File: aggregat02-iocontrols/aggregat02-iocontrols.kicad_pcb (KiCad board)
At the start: 2 copper layers, 45.7 x 101.9 mm, 75 parts, among them Q2 Q_NPN_BEC

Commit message: v1.0"
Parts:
- removed D2: LED, LED_THT:LED_D3.0mm
- added J1: Conn_01x04, Connector_PinHeader_2.54mm:PinHeader_1x04_P2.54mm_Vertical, B.Cu at (78.7, 69.3)
- added J10: Conn_01x01, Connector_PinHeader_2.54mm:PinHeader_1x01_P2.54mm_Vertical, B.Cu at (81.5, 117.3)
- added J11: Conn_01x01, Connector_PinHeader_2.54mm:PinHeader_1x01_P2.54mm_Vertical, B.Cu at (71.9, 127.0)
- added J12: Conn_01x01, Connector_PinHeader_2.54mm:PinHeader_1x01_P2.54mm_Vertical, B.Cu at (81.8, 127.0)
- added J13: Conn_01x01, Connector_PinHeader_2.54mm:PinHeader_1x01_P2.54mm_Vertical, B.Cu at (71.9, 137.2)
- added J14: Conn_01x01, Connector_PinHeader_2.54mm:PinHeader_1x01_P2.54mm_Vertical, B.Cu at (81.8, 137.2)
- added J15: Conn_01x15, Connector_Molex:Molex_PicoBlade_53047-1510_1x15_P1.25mm_Vertical, B.Cu at (89.2, 57.7)
- added J16: Conn_01x15, Connector_Molex:Molex_PicoBlade_53047-1510_1x15_P1.25mm_Vertical, B.Cu at (88.9, 87.1)
- added J17: Conn_01x03, Connector_PinHeader_2.54mm:PinHeader_1x02_P2.54mm_Vertical, B.Cu at (54.1, 96.8)
- added J18: Conn_01x03, Connector_Molex:Molex_PicoBlade_53047-0310_1x03_P1.25mm_Vertical, B.Cu at (52.8, 55.6)
- added J19: Conn_01x01, Connector_PinHeader_2.54mm:PinHeader_1x01_P2.54mm_Vertical, B.Cu at (56.1, 49.0)
- added J2: Conn_01x04, Connector_PinHeader_2.54mm:PinHeader_1x04_P2.54mm_Vertical, B.Cu at (79.0, 54.6)
- added J3: Conn_01x08, Connector_PinHeader_2.54mm:PinHeader_1x08_P2.54mm_Vertical, B.Cu at (78.7, 86.6)
- added J4: Conn_01x01, Connector_PinHeader_2.54mm:PinHeader_1x01_P2.54mm_Vertical, B.Cu at (51.3, 115.6)
- added J5: Conn_01x01, Connector_PinHeader_2.54mm:PinHeader_1x01_P2.54mm_Vertical, B.Cu at (51.3, 125.5)
- added J6: Conn_01x01, Connector_PinHeader_2.54mm:PinHeader_1x01_P2.54mm_Vertical, B.Cu at (51.3, 135.4)
- added J7: Conn_01x01, Connector_PinHeader_2.54mm:PinHeader_1x01_P2.54mm_Vertical, B.Cu at (79.0, 50.5)
- added J8: Conn_01x01, Connector_PinHeader_2.54mm:PinHeader_1x01_P2.54mm_Vertical, B.Cu at (88.4, 50.8)
- added J9: Conn_01x01, Connector_PinHeader_2.54mm:PinHeader_1x01_P2.54mm_Vertical, B.Cu at (71.9, 117.1)
- added LD11: LED, LED_THT:LED_D3.0mm, F.Cu at (70.9, 112.8)
- added LD12: LED, LED_THT:LED_D3.0mm, F.Cu at (80.8, 112.8)
- added LD21: LED, LED_THT:LED_D3.0mm, F.Cu at (70.9, 122.7)
- added LD22: LED, LED_THT:LED_D3.0mm, F.Cu at (80.8, 122.7)
- added LD31: LED, LED_THT:LED_D3.0mm, F.Cu at (70.9, 132.6)
- added LD32: LED, LED_THT:LED_D3.0mm, F.Cu at (80.8, 132.6)
- added LD_MTR1: LED, LED_THT:LED_D3.0mm, F.Cu at (79.5, 43.7)
- added Q1: Q_NPN_BEC, Package_TO_SOT_SMD:SOT-23, B.Cu at (84.1, 44.7)
- added Q3: Q_NPN_BEC, Package_TO_SOT_SMD:SOT-23, B.Cu at (74.2, 111.3)
- added Q4: Q_NPN_BEC, Package_TO_SOT_SMD:SOT-23, B.Cu at (84.1, 111.5)
- added Q5: Q_NPN_BEC, Package_TO_SOT_SMD:SOT-23, B.Cu at (74.2, 121.2)
- added Q6: Q_NPN_BEC, Package_TO_SOT_SMD:SOT-23, B.Cu at (84.1, 121.2)
- added Q7: Q_NPN_BEC, Package_TO_SOT_SMD:SOT-23, B.Cu at (74.2, 131.3)
- added Q8: Q_NPN_BEC, Package_TO_SOT_SMD:SOT-23, B.Cu at (84.1, 131.3)
- added R42: R 47k 1% 1/8, Resistor_SMD:R_0805_2012Metric_Pad1.15x1.40mm_HandSolder, B.Cu at (85.1, 50.6)
- added R43: R 100k 1% 1/8, Resistor_SMD:R_0805_2012Metric_Pad1.15x1.40mm_HandSolder, B.Cu at (84.1, 47.5)
- added R44: R 270 1% 1/8, Resistor_SMD:R_0805_2012Metric_Pad1.15x1.40mm_HandSolder, F.Cu at (74.2, 47.5)
- added R45: R 47k 1% 1/8, Resistor_SMD:R_0805_2012Metric_Pad1.15x1.40mm_HandSolder, B.Cu at (75.2, 117.1)
- added R46: R 100k 1% 1/8, Resistor_SMD:R_0805_2012Metric_Pad1.15x1.40mm_HandSolder, B.Cu at (74.2, 114.0)
- added R47: R 270 1% 1/8, Resistor_SMD:R_0805_2012Metric_Pad1.15x1.40mm_HandSolder, F.Cu at (66.0, 110.7)
- added R48: R 47k 1% 1/8, Resistor_SMD:R_0805_2012Metric_Pad1.15x1.40mm_HandSolder, B.Cu at (85.1, 117.3)
- added R49: R 100k 1% 1/8, Resistor_SMD:R_0805_2012Metric_Pad1.15x1.40mm_HandSolder, B.Cu at (84.1, 114.3)
- added R50: R 270 1% 1/8, Resistor_SMD:R_0805_2012Metric_Pad1.15x1.40mm_HandSolder, F.Cu at (74.9, 109.7)
- added R51: R 47k 1% 1/8, Resistor_SMD:R_0805_2012Metric_Pad1.15x1.40mm_HandSolder, B.Cu at (75.2, 127.0)
- added R52: R 100k 1% 1/8, Resistor_SMD:R_0805_2012Metric_Pad1.15x1.40mm_HandSolder, B.Cu at (74.2, 124.0)
- added R53: R 270 1% 1/8, Resistor_SMD:R_0805_2012Metric_Pad1.15x1.40mm_HandSolder, F.Cu at (66.0, 121.2)
- added R54: R 47k 1% 1/8, Resistor_SMD:R_0805_2012Metric_Pad1.15x1.40mm_HandSolder, B.Cu at (85.1, 127.0)
- added R55: R 100k 1% 1/8, Resistor_SMD:R_0805_2012Metric_Pad1.15x1.40mm_HandSolder, B.Cu at (84.1, 124.0)
- added R56: R 270 1% 1/8, Resistor_SMD:R_0805_2012Metric_Pad1.15x1.40mm_HandSolder, F.Cu at (74.9, 120.1)
- added R57: R 47k 1% 1/8, Resistor_SMD:R_0805_2012Metric_Pad1.15x1.40mm_HandSolder, B.Cu at (75.2, 137.2)
- added R58: R 100k 1% 1/8, Resistor_SMD:R_0805_2012Metric_Pad1.15x1.40mm_HandSolder, B.Cu at (74.2, 134.1)
- added R59: R 270 1% 1/8, Resistor_SMD:R_0805_2012Metric_Pad1.15x1.40mm_HandSolder, F.Cu at (66.0, 131.1)
- added R60: R 47k 1% 1/8, Resistor_SMD:R_0805_2012Metric_Pad1.15x1.40mm_HandSolder, B.Cu at (85.1, 137.2)
- added R61: R 100k 1% 1/8, Resistor_SMD:R_0805_2012Metric_Pad1.15x1.40mm_HandSolder, B.Cu at (84.1, 134.1)
- added R62: R 270 1% 1/8, Resistor_SMD:R_0805_2012Metric_Pad1.15x1.40mm_HandSolder, F.Cu at (74.7, 130.0)
- Q2, R41: moved to B.Cu
- R39: value R -> R 270 1% 1/8; moved to F.Cu
- R40: value R 270 1% 1/8 -> R 47k 1% 1/8; moved to B.Cu
- moved REF** 37.4 mm to (90.4, 141.7)
- moved REF** 36.6 mm to (53.8, 141.7)
- moved C17 14.5 mm to (54.6, 112.5), turned to 90 degrees
- moved C19 14.5 mm to (54.6, 132.3), turned to 90 degrees
- moved C18 14.5 mm to (54.6, 122.4), turned to 90 degrees
- moved R34 14.2 mm to (55.6, 109.5), turned to 0 degrees
- moved R38 14.2 mm to (55.6, 129.3), turned to 0 degrees
- moved R36 14.1 mm to (55.6, 119.6), turned to 0 degrees
- moved REF** 13.5 mm to (72.6, 81.8)
- moved R33 13.5 mm to (55.6, 115.6), turned to 0 degrees
- moved R35 13.5 mm to (55.6, 125.5), turned to 0 degrees
- moved R37 13.4 mm to (55.6, 135.4), turned to 0 degrees
- moved R40 9.76 mm to (75.2, 50.5)
- moved R41 7.94 mm to (74.2, 47.5), turned to 180 degrees
- moved R39 7.13 mm to (68.3, 49.5), turned to 270 degrees
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- renumbered D1 to LD_PWR1
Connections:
- R40 pad 2: LED_1 -> LED_PWR
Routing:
- net SW_PLUS2: track 2.03 -> 69.9 mm
- net +3V3: track 82.4 -> 143.7 mm
- net SW_PLUS1: track 2.02 -> 60.9 mm
- net SW_CENTER: track 2.04 -> 53.4 mm
- net LED31: track 0.00 -> 50.3 mm
- net LED21: track 0.00 -> 42.9 mm
- net LED32: track 0.00 -> 41.0 mm
- net LED11: track 0.00 -> 34.3 mm
- net LED22: track 0.00 -> 33.8 mm
- net SW_CFG_4: track 6.84 -> 33.8 mm, vias 1 -> 0
- net SW_CFG_2: track 6.84 -> 33.4 mm, vias 1 -> 0
- net SW_CFG_1: track 6.84 -> 32.8 mm, vias 1 -> 0
- net LED12: track 0.00 -> 25.6 mm
- net SW_CFG_3: track 7.42 -> 33.0 mm, vias 1 -> 0
- net SW_CH_1: track 1.83 -> 23.7 mm, vias 1 -> 0
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- added copper zone on B.Cu, net GNDREF
- added copper zone on F.Cu, net GNDREF
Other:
- board size 45.7 x 101.9 mm -> 45.7 x 107.4 mm
- board text added: "Aggregat 02 iocontrols v1.0 © 2020 ICST / ZHdK"
- board text added: "designed by filou.se"

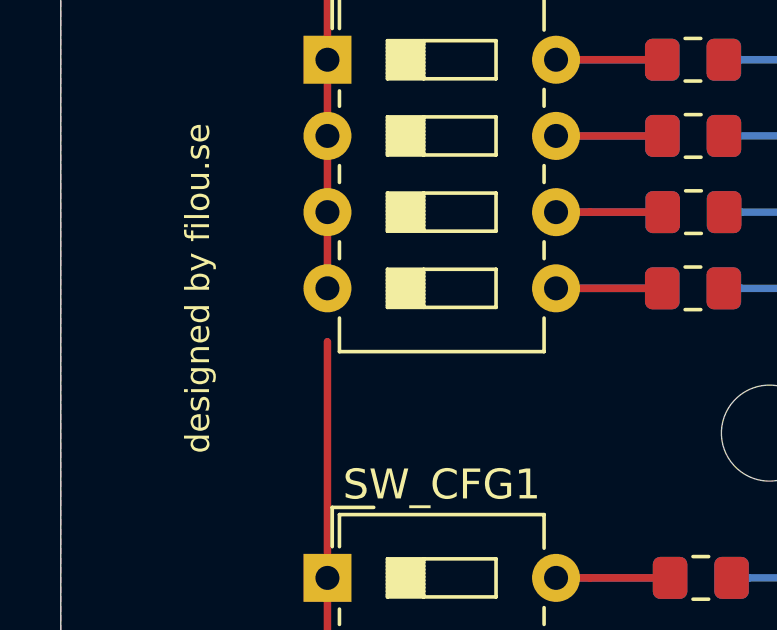
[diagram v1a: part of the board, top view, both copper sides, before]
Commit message: gitignore and bugfix (non-connected 3V3)
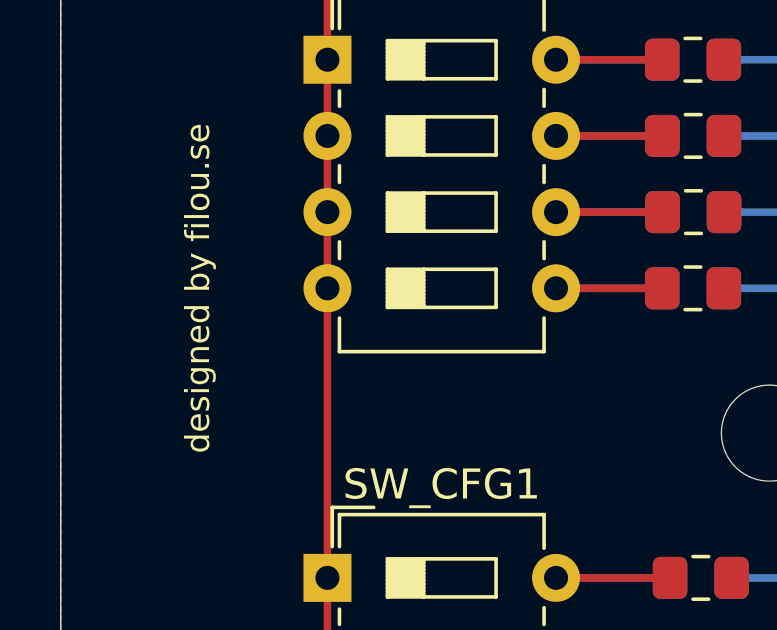
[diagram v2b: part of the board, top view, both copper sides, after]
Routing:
- net +3V3: track 143.7 -> 145.5 mm
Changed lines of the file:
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@@
     (thickness 1.6)
     (drawings 16)
-    (tracks 397)
+    (tracks 398)
     (zones 0)
     (modules 128)
@@
   (segment (start 73.218 123.877) (end 73.143 123.952) (width 0.25) (layer B.Cu) (net 1))
   (segment (start 73.218 122.158) (end 73.218 123.877) (width 0.25) (layer B.Cu) (net 1))
+  (segment (start 63.976 42.312) (end 63.976 48.112) (width 0.25) (layer F.Cu) (net 1))
   (segment (start 75.701 86.614) (end 78.74 86.614) (width 0.25) (layer F.Cu) (net 2))
   (segment (start 71.958 86.614) (end 78.74 86.614) (width 0.25) (layer B.Cu) (net 2))
@@
   (segment (start 66.04 130.039) (end 73.642 130.039) (width 0.25) (layer F.Cu) (net 18))
   (segment (start 54.102 96.774) (end 57.912 96.774) (width 0.25) (layer F.Cu) (net 18))
+  (segment (start 56.896 55.626) (end 57.912 54.61) (width 0.25) (layer F.Cu) (net 18))
+  (segment (start 52.832 55.626) (end 56.896 55.626) (width 0.25) (layer F.Cu) (net 18))
+  (segment (start 57.912 76.962) (end 57.912 78.74) (width 0.25) (layer F.Cu) (net 18))
   (segment (start 71.129 69.342) (end 71.704 69.342) (width 0.25) (layer B.Cu) (net 19))
   (segment (start 75.692 69.342) (end 78.74 69.342) (width 0.25) (layer F.Cu) (net 19))
@@
   (segment (start 66.66337 62.23) (end 69.07 62.23) (width 0.25) (layer F.Cu) (net 34))
   (segment (start 65.532 62.23) (end 66.66337 62.23) (width 0.25) (layer F.Cu) (net 34))
-  (segment (start 63.976 42.312) (end 63.976 48.112) (width 0.25) (layer F.Cu) (net 1))
-  (segment (start 56.896 55.626) (end 57.912 54.61) (width 0.25) (layer F.Cu) (net 18))
-  (segment (start 52.832 55.626) (end 56.896 55.626) (width 0.25) (layer F.Cu) (net 18))
   (segment (start 59.226 48.112) (end 59.976 48.112) (width 0.25) (layer F.Cu) (net 35))
   (segment (start 52.832 53.126) (end 52.832 52.476) (width 0.25) (layer F.Cu) (net 35))

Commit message: fixes
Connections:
- J16 pad 5: SW_CENTER -> Net-(J16-Pad5)
- J16 pad 6: SW_PLUS1 -> GNDREF
- J16 pad 7: SW_PLUS2 -> SW_CENTER
- J16 pad 8: Net-(J16-Pad8) -> SW_PLUS1
- J16 pad 9: GNDREF -> SW_PLUS2
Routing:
- net SW_PLUS2: track 69.9 -> 70.7 mm
- net SW_CENTER: track 53.4 -> 54.2 mm
- net SW_PLUS1: track 60.9 -> 61.7 mm
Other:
- board text added: "Aggregat 02 iocontrols v1.1 © 2020 ICST / ZHdK"
- board text removed: "Aggregat 02 iocontrols v1.0 © 2020 ICST / ZHdK"

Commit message: v1.2
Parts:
- removed J15, J16: Conn_01x15, Connector_Molex:Molex_PicoBlade_53047-1510_1x15_P1.25mm_Vertical
- removed J18: Conn_01x03, Connector_Molex:Molex_PicoBlade_53047-0310_1x03_P1.25mm_Vertical
- removed J8: Conn_01x01, Connector_PinHeader_2.54mm:PinHeader_1x01_P2.54mm_Vertical
- added CN1: Conn_01x15, Connector_PinHeader_2.54mm:PinHeader_1x15_P2.54mm_Vertical, B.Cu at (90.2, 52.1)
- added CN2: Conn_01x15, Connector_PinHeader_2.54mm:PinHeader_1x15_P2.54mm_Vertical, B.Cu at (90.2, 97.3)
- moved J17 0.51 mm to (54.6, 96.8)
- moved REF** 0.25 mm to (90.2, 141.7)
- renumbered J19 to NRST
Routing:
- net LED31: track 50.3 -> 25.1 mm
- net LED32: track 41.0 -> 16.1 mm
- net LED22: track 33.8 -> 13.5 mm
- net LED21: track 42.9 -> 22.8 mm
- net LED12: track 25.6 -> 16.3 mm
- net SW_CFG_4: track 33.8 -> 24.6 mm
- net LED11: track 34.3 -> 25.2 mm
- net SW_CFG_2: track 33.4 -> 24.6 mm
- net SW_CFG_3: track 33.0 -> 24.6 mm
- net SW_CFG_1: track 32.8 -> 25.6 mm
- net SW_NRST: track 17.5 -> 10.8 mm
- net SW_CFG_8: track 28.7 -> 22.0 mm
- net LED_MOTOR: track 10.8 -> 5.28 mm
- net SW_CFG_7: track 27.9 -> 22.6 mm
- net +3V3: track 145.5 -> 140.9 mm
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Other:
- board text added: "3V3"
- board text added: "Aggregat 02 iocontrols v1.2 © 2020 ICST / ZHdK"
- board text added: "BTN"
- board text added: "CFG1- 4"
- board text added: "CFG5-8"
- board text added: "CH"
- board text added: "GND"
- board text added: "ID"
- board text added: "LED"
- board text added: "NC"
- board text removed: "Aggregat 02 iocontrols v1.1 © 2020 ICST / ZHdK"

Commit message: dimensions
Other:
- board text added: "NRST"
